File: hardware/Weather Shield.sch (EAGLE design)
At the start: 44 parts, among them Q1 BSS138, Q2 BSS138, U1 ARDUINO_R3_SHIELD, U2 3.3V MIC5219, U4 MPL3115A2LGA8, U5 HTU21D, U7 GP-635T, U8 TEMT6000

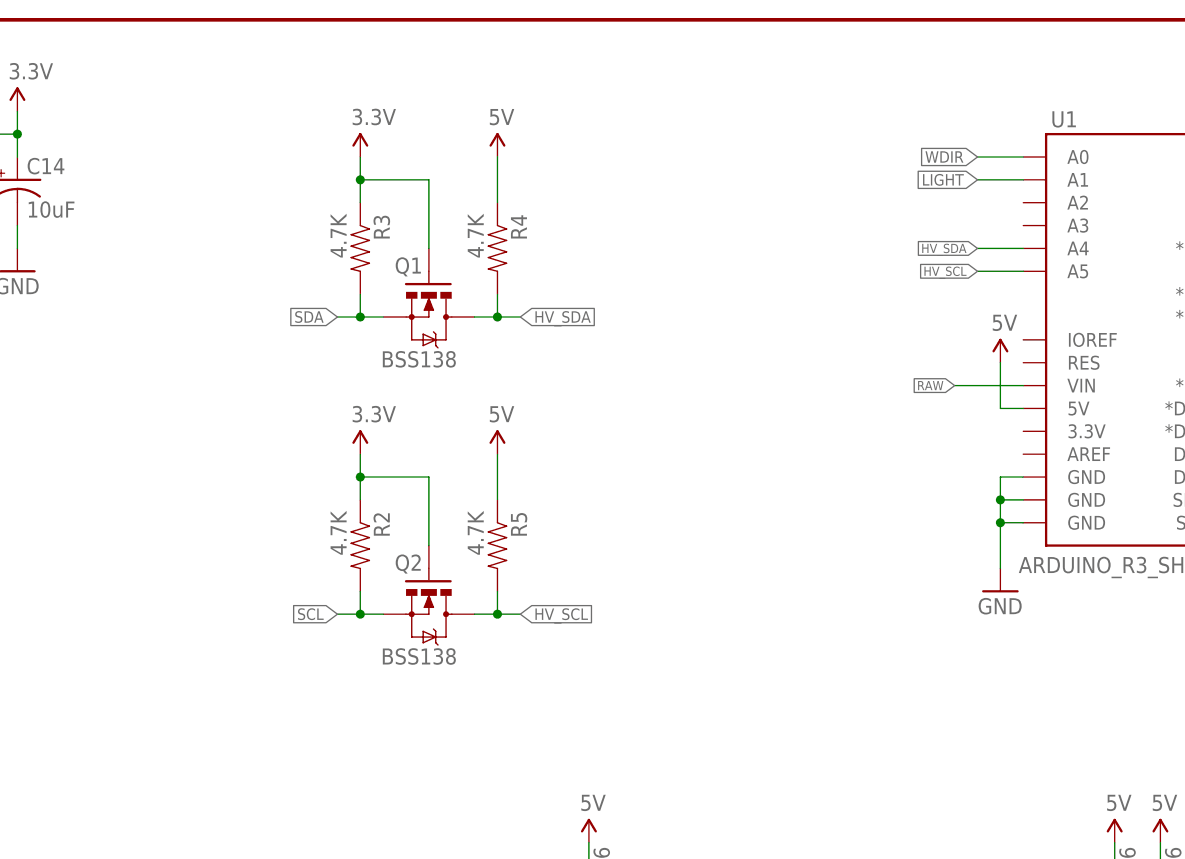
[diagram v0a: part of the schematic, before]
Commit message: Added analog sense on VIN/Batt level.
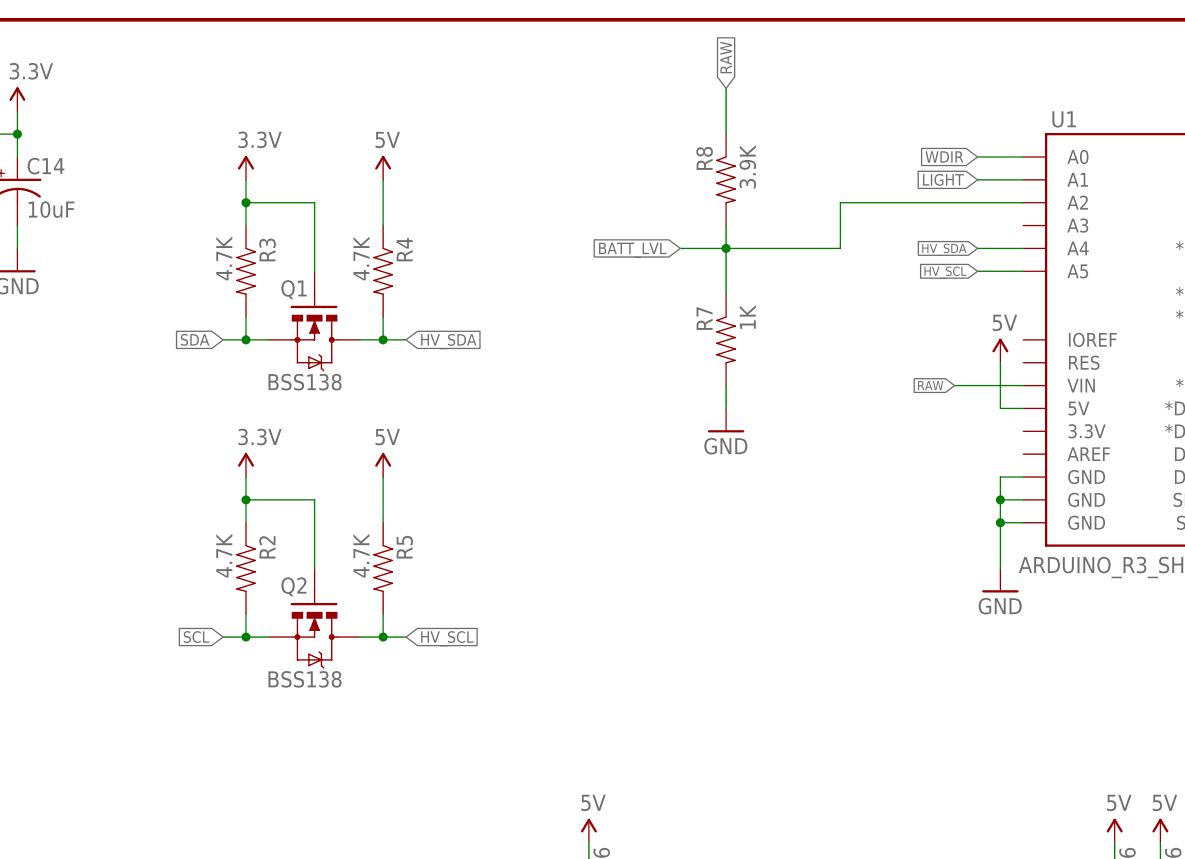
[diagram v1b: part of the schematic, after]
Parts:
- added R7: 1K, SparkFun:RESISTOR0603-RES
- added R8: 3.9K, SparkFun:RESISTOR0603-RES
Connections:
- new net BATT_LVL: R7.1, R8.2, U1.A2
- net GND: now also R7.2
- net RAW: now also R8.1
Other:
- moved on the sheet: Q1, Q2, R2, R3, R4, R5

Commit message: Added power ctl to GPS and backup battery connection.
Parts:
- added JP1: Ext Batt, SparkFun-Connectors:M01PTH
- added LOGO1: OSHW-LOGOM, SparkFun-Aesthetics:OSHW-LOGOM
- added R9: 1K, SparkFun:RESISTOR0603-RES
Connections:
- new net 3V_PWR_CTL: R9.2, U7.1
- net PWR_CTL: now also R9.1; no longer U7.1
- net V_BATT: now also JP1.1
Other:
- moved on the sheet: S2

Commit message: Tweaked schematic labels and connector for backup battery.
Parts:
- removed JP1: Ext Batt, SparkFun-Connectors:M01PTH
- added JP2: M02PTH, SparkFun-Connectors:M02PTH
- R9: value 1K -> 4.7K
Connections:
- net GND: now also JP2.1
- net V_BATT: now also JP2.2; no longer JP1.1
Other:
- note added: "1.5 to 3.5V"
- moved on the sheet: S2
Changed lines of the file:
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@@
 <part name="GND28" library="SparkFun" deviceset="GND" device=""/>
 <part name="LOGO1" library="SparkFun-Aesthetics" deviceset="OSHW-LOGO" device="M"/>
-<part name="R9" library="SparkFun" deviceset="RESISTOR" device="0603-RES" value="1K"/>
-<part name="JP1" library="SparkFun-Connectors" deviceset="M01" device="PTH" value="Ext Batt"/>
+<part name="R9" library="SparkFun" deviceset="RESISTOR" device="0603-RES" value="4.7K"/>
+<part name="JP2" library="SparkFun-Connectors" deviceset="M02" device="PTH"/>
+<part name="GND5" library="SparkFun" deviceset="GND" device=""/>
 </parts>
 <sheets>
@@
 <text x="116.84" y="101.6" size="2.54" layer="102">Rain (optional)</text>
 <text x="241.3" y="91.44" size="1.27" layer="91">This will not work...</text>
+<text x="20.574" y="38.862" size="1.778" layer="97">1.5 to 3.5V</text>
 </plain>
 <instances>
@@
 <instance part="P+14" gate="1" x="104.14" y="40.64"/>
 <instance part="GND20" gate="1" x="104.14" y="7.62"/>
-<instance part="S2" gate="G$1" x="25.4" y="25.4" rot="MR0"/>
+<instance part="S2" gate="G$1" x="25.4" y="17.78" rot="MR0"/>
 <instance part="GND13" gate="1" x="53.34" y="12.7"/>
 <instance part="P+5" gate="1" x="53.34" y="35.56"/>
@@
 <instance part="LOGO1" gate="G$1" x="134.62" y="10.16"/>
 <instance part="R9" gate="G$1" x="27.94" y="45.72" rot="MR180"/>
-<instance part="JP1" gate="G$1" x="12.7" y="38.1"/>
+<instance part="JP2" gate="G$1" x="12.7" y="35.56"/>
+<instance part="GND5" gate="1" x="22.86" y="30.48"/>
 </instances>
 <busses>
@@
 <pinref part="GND28" gate="1" pin="GND"/>
 </segment>
+<segment>
+<pinref part="JP2" gate="G$1" pin="1"/>
+<wire x1="20.32" y1="35.56" x2="22.86" y2="35.56" width="0.1524" layer="91"/>
+<wire x1="22.86" y1="35.56" x2="22.86" y2="33.02" width="0.1524" layer="91"/>
+<pinref part="GND5" gate="1" pin="GND"/>
+</segment>
 </net>
 <net name="STAT2" class="0">
@@
 <segment>
 <wire x1="213.36" y1="167.64" x2="223.52" y2="167.64" width="0.1524" layer="91"/>
-<label x="215.9" y="167.64" size="1.778" layer="95"/>
 <pinref part="U1" gate="G$1" pin="TX"/>
+<label x="223.52" y="167.64" size="1.27" layer="95" xref="yes"/>
 </segment>
 <segment>
 <pinref part="S2" gate="G$1" pin="1"/>
-<wire x1="20.32" y1="30.48" x2="10.16" y2="30.48" width="0.1524" layer="91"/>
-<label x="10.16" y="30.48" size="1.778" layer="95"/>
+<wire x1="20.32" y1="22.86" x2="10.16" y2="22.86" width="0.1524" layer="91"/>
+<label x="10.16" y="22.86" size="1.778" layer="95"/>
 </segment>
 </net>
@@
 <segment>
 <pinref part="U1" gate="G$1" pin="VIN"/>
-<wire x1="187.96" y1="144.78" x2="180.34" y2="144.78" width="0.1524" layer="91"/>
-<label x="180.34" y="144.78" size="1.016" layer="95" rot="R180" xref="yes"/>
+<wire x1="187.96" y1="144.78" x2="182.88" y2="144.78" width="0.1524" layer="91"/>
+<label x="182.88" y="144.78" size="1.27" layer="95" rot="R180" xref="yes"/>
 </segment>
 <segment>
@@
 <segment>
 <wire x1="213.36" y1="170.18" x2="223.52" y2="170.18" width="0.1524" layer="91"/>
-<label x="215.9" y="170.18" size="1.778" layer="95"/>
 <pinref part="U1" gate="G$1" pin="RX"/>
+<label x="223.52" y="170.18" size="1.27" layer="95" xref="yes"/>
 </segment>
 <segment>
 <pinref part="S2" gate="G$1" pin="4"/>
-<wire x1="20.32" y1="22.86" x2="10.16" y2="22.86" width="0.1524" layer="91"/>
-<label x="10.16" y="22.86" size="1.778" layer="95"/>
+<wire x1="20.32" y1="15.24" x2="10.16" y2="15.24" width="0.1524" layer="91"/>
+<label x="10.16" y="15.24" size="1.778" layer="95"/>
 </segment>
 </net>
@@
 <segment>
 <pinref part="U7" gate="G$1" pin="4"/>
-<wire x1="33.02" y1="22.86" x2="55.88" y2="22.86" width="0.1524" layer="91"/>
+<wire x1="35.56" y1="22.86" x2="55.88" y2="22.86" width="0.1524" layer="91"/>
 <label x="40.64" y="22.86" size="1.778" layer="95"/>
-<wire x1="33.02" y1="22.86" x2="33.02" y2="20.32" width="0.1524" layer="91"/>
+<wire x1="35.56" y1="22.86" x2="35.56" y2="12.7" width="0.1524" layer="91"/>
 <pinref part="S2" gate="G$1" pin="5"/>
-<wire x1="33.02" y1="20.32" x2="30.48" y2="20.32" width="0.1524" layer="91"/>
+<wire x1="35.56" y1="12.7" x2="30.48" y2="12.7" width="0.1524" layer="91"/>
 </segment>
 </net>
@@
 <wire x1="33.02" y1="25.4" x2="55.88" y2="25.4" width="0.1524" layer="91"/>
 <label x="40.64" y="25.4" size="1.778" layer="95"/>
-<wire x1="33.02" y1="25.4" x2="33.02" y2="27.94" width="0.1524" layer="91"/>
+<wire x1="33.02" y1="25.4" x2="33.02" y2="20.32" width="0.1524" layer="91"/>
+<wire x1="33.02" y1="20.32" x2="30.48" y2="20.32" width="0.1524" layer="91"/>
 <pinref part="S2" gate="G$1" pin="2"/>
-<wire x1="33.02" y1="27.94" x2="30.48" y2="27.94" width="0.1524" layer="91"/>
 </segment>
 </net>
@@
 <label x="40.64" y="27.94" size="1.778" layer="95"/>
 <wire x1="35.56" y1="27.94" x2="35.56" y2="38.1" width="0.1524" layer="91"/>
-<pinref part="JP1" gate="G$1" pin="1"/>
 <wire x1="35.56" y1="38.1" x2="20.32" y2="38.1" width="0.1524" layer="91"/>
+<pinref part="JP2" gate="G$1" pin="2"/>
 </segment>
 </net>
@@
 <pinref part="U1" gate="G$1" pin="*D6"/>
 <wire x1="213.36" y1="152.4" x2="223.52" y2="152.4" width="0.1524" layer="91"/>
-<label x="215.9" y="152.4" size="1.27" layer="95"/>
+<label x="223.52" y="152.4" size="1.27" layer="95" xref="yes"/>
 </segment>
 <segment>
@@
 <segment>
 <pinref part="S2" gate="G$1" pin="3"/>
-<wire x1="20.32" y1="25.4" x2="10.16" y2="25.4" width="0.1524" layer="91"/>
-<label x="10.16" y="25.4" size="1.778" layer="95"/>
-</segment>
-<segment>
-<wire x1="213.36" y1="157.48" x2="223.52" y2="157.48" width="0.1524" layer="91"/>
-<label x="215.9" y="157.48" size="1.778" layer="95"/>
-<pinref part="U1" gate="G$1" pin="D4"/>
-</segment>
-</net>
-<net name="GRXI" class="0">
-<segment>
-<pinref part="S2" gate="G$1" pin="6"/>
 <wire x1="20.32" y1="17.78" x2="10.16" y2="17.78" width="0.1524" layer="91"/>
 <label x="10.16" y="17.78" size="1.778" layer="95"/>
 </segment>
 <segment>
+<wire x1="213.36" y1="157.48" x2="223.52" y2="157.48" width="0.1524" layer="91"/>
+<pinref part="U1" gate="G$1" pin="D4"/>
+<label x="223.52" y="157.48" size="1.27" layer="95" xref="yes"/>
+</segment>
+</net>
+<net name="GRXI" class="0">
+<segment>
+<pinref part="S2" gate="G$1" pin="6"/>
+<wire x1="20.32" y1="10.16" x2="10.16" y2="10.16" width="0.1524" layer="91"/>
+<label x="10.16" y="10.16" size="1.778" layer="95"/>
+</segment>
+<segment>
 <wire x1="213.36" y1="154.94" x2="223.52" y2="154.94" width="0.1524" layer="91"/>
-<label x="215.9" y="154.94" size="1.778" layer="95"/>
 <pinref part="U1" gate="G$1" pin="*D5"/>
+<label x="223.52" y="154.94" size="1.27" layer="95" xref="yes"/>
 </segment>
 </net>
@@
 <pinref part="U1" gate="G$1" pin="A4"/>
 <wire x1="182.88" y1="160.02" x2="187.96" y2="160.02" width="0.1524" layer="91"/>
-<label x="182.88" y="160.02" size="1.016" layer="95" rot="R180" xref="yes"/>
+<label x="182.88" y="160.02" size="1.27" layer="95" rot="R180" xref="yes"/>
 </segment>
 <segment>
@@
 <wire x1="182.88" y1="157.48" x2="187.96" y2="157.48" width="0.1524" layer="91"/>
 <pinref part="U1" gate="G$1" pin="A5"/>
-<label x="182.88" y="157.48" size="1.016" layer="95" rot="R180" xref="yes"/>
-</segment>
-<segment>
+<label x="182.88" y="157.48" size="1.27" layer="95" rot="R180" xref="yes"/>
+</segment>
+<segment>

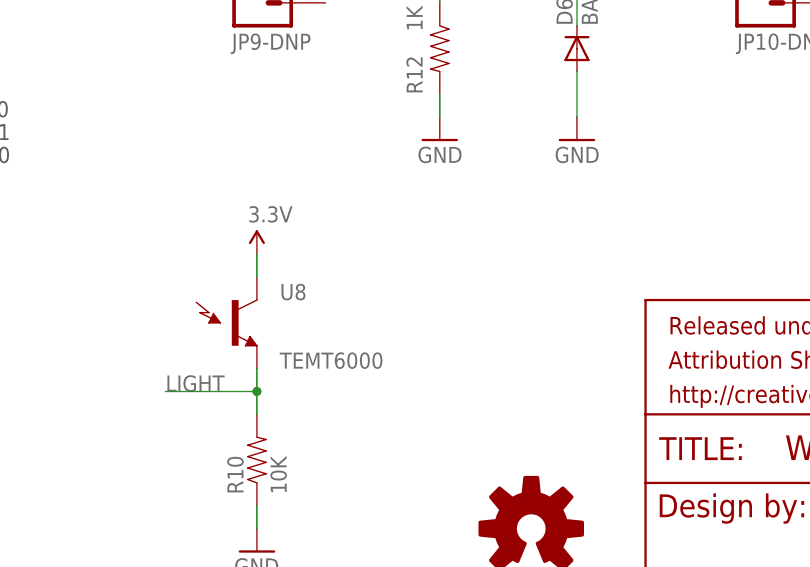
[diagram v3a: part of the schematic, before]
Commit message: Added support for smaller, cheaper ALS-PT19 light sensor.
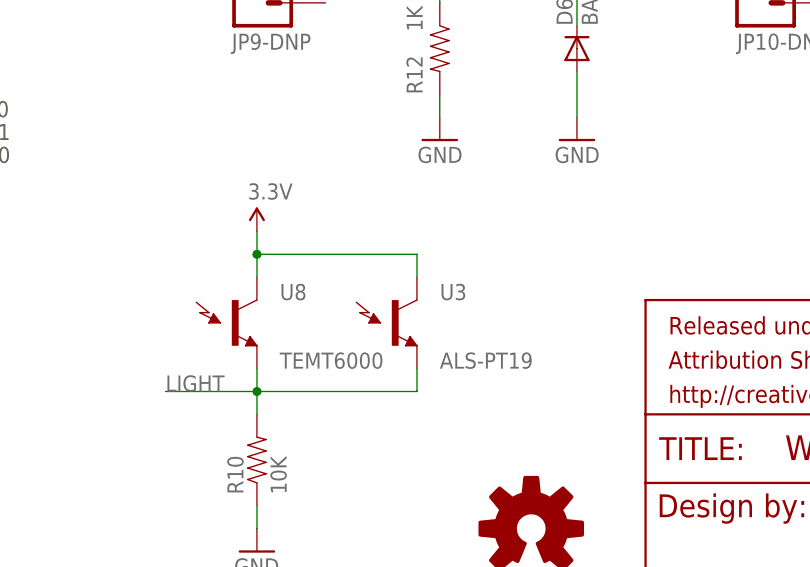
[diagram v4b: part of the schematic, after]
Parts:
- added U3: ALS-PT19, SparkFun-Sensors:LIGHTSENSORALS
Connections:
- net 3.3V: now also U3.C1
- net LIGHT: now also U3.E1
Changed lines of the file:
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@@
 <part name="JP2" library="SparkFun-Connectors" deviceset="M02" device="PTH"/>
 <part name="GND5" library="SparkFun" deviceset="GND" device=""/>
+<part name="U3" library="SparkFun-Sensors" deviceset="LIGHTSENSOR" device="ALS" value="ALS-PT19"/>
 </parts>
 <sheets>
@@
 <instance part="P+10" gate="1" x="20.32" y="78.74"/>
 <instance part="P+13" gate="1" x="33.02" y="121.92"/>
-<instance part="P+14" gate="1" x="104.14" y="40.64"/>
+<instance part="P+14" gate="1" x="104.14" y="43.18"/>
 <instance part="GND20" gate="1" x="104.14" y="7.62"/>
 <instance part="S2" gate="G$1" x="25.4" y="17.78" rot="MR0"/>
@@
 <instance part="JP2" gate="G$1" x="12.7" y="35.56"/>
 <instance part="GND5" gate="1" x="22.86" y="30.48"/>
+<instance part="U3" gate="G$1" x="119.38" y="33.02"/>
 </instances>
 <busses>
@@
 <pinref part="U8" gate="G$1" pin="C1"/>
 <pinref part="P+14" gate="1" pin="VCC"/>
+<wire x1="104.14" y1="43.18" x2="104.14" y2="40.64" width="0.1524" layer="91"/>
+<pinref part="U3" gate="G$1" pin="C1"/>
 <wire x1="104.14" y1="40.64" x2="104.14" y2="38.1" width="0.1524" layer="91"/>
+<wire x1="104.14" y1="40.64" x2="121.92" y2="40.64" width="0.1524" layer="91"/>
+<wire x1="121.92" y1="40.64" x2="121.92" y2="38.1" width="0.1524" layer="91"/>
+<junction x="104.14" y="40.64"/>
 </segment>
 <segment>
@@
 <junction x="104.14" y="25.4"/>
 <label x="93.98" y="25.4" size="1.778" layer="95"/>
-</segment>
-<segment>
+<pinref part="U3" gate="G$1" pin="E1"/>
+<wire x1="121.92" y1="27.94" x2="121.92" y2="25.4" width="0.1524" layer="91"/>
+<wire x1="121.92" y1="25.4" x2="104.14" y2="25.4" width="0.1524" layer="91"/>
+</segment>
+<segment>
